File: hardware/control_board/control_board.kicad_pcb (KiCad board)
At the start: 2 copper layers, 80 x 80 mm, 126 parts, among them J1 SWD, J2 Panel, J3 Aux, J4 6.5/2mm, J5 USB_C, J6 RTD, J7 TC, J8 Conn_01x01, J9 Conn_01x01, Q1 2N7002A, Q2 IRF1018ESTRLPBF, SW1 Reset, SW2 Power, U1 STM32F103C8T6, U2 LMR38010SDDAR, U3 TLV76133DCYR, U4 USBLC6-2SC6, U5 MAX6675, U6 MCP6N11T-005E, U7 MCP6001T, U8 TLP183, Y1 8MHz

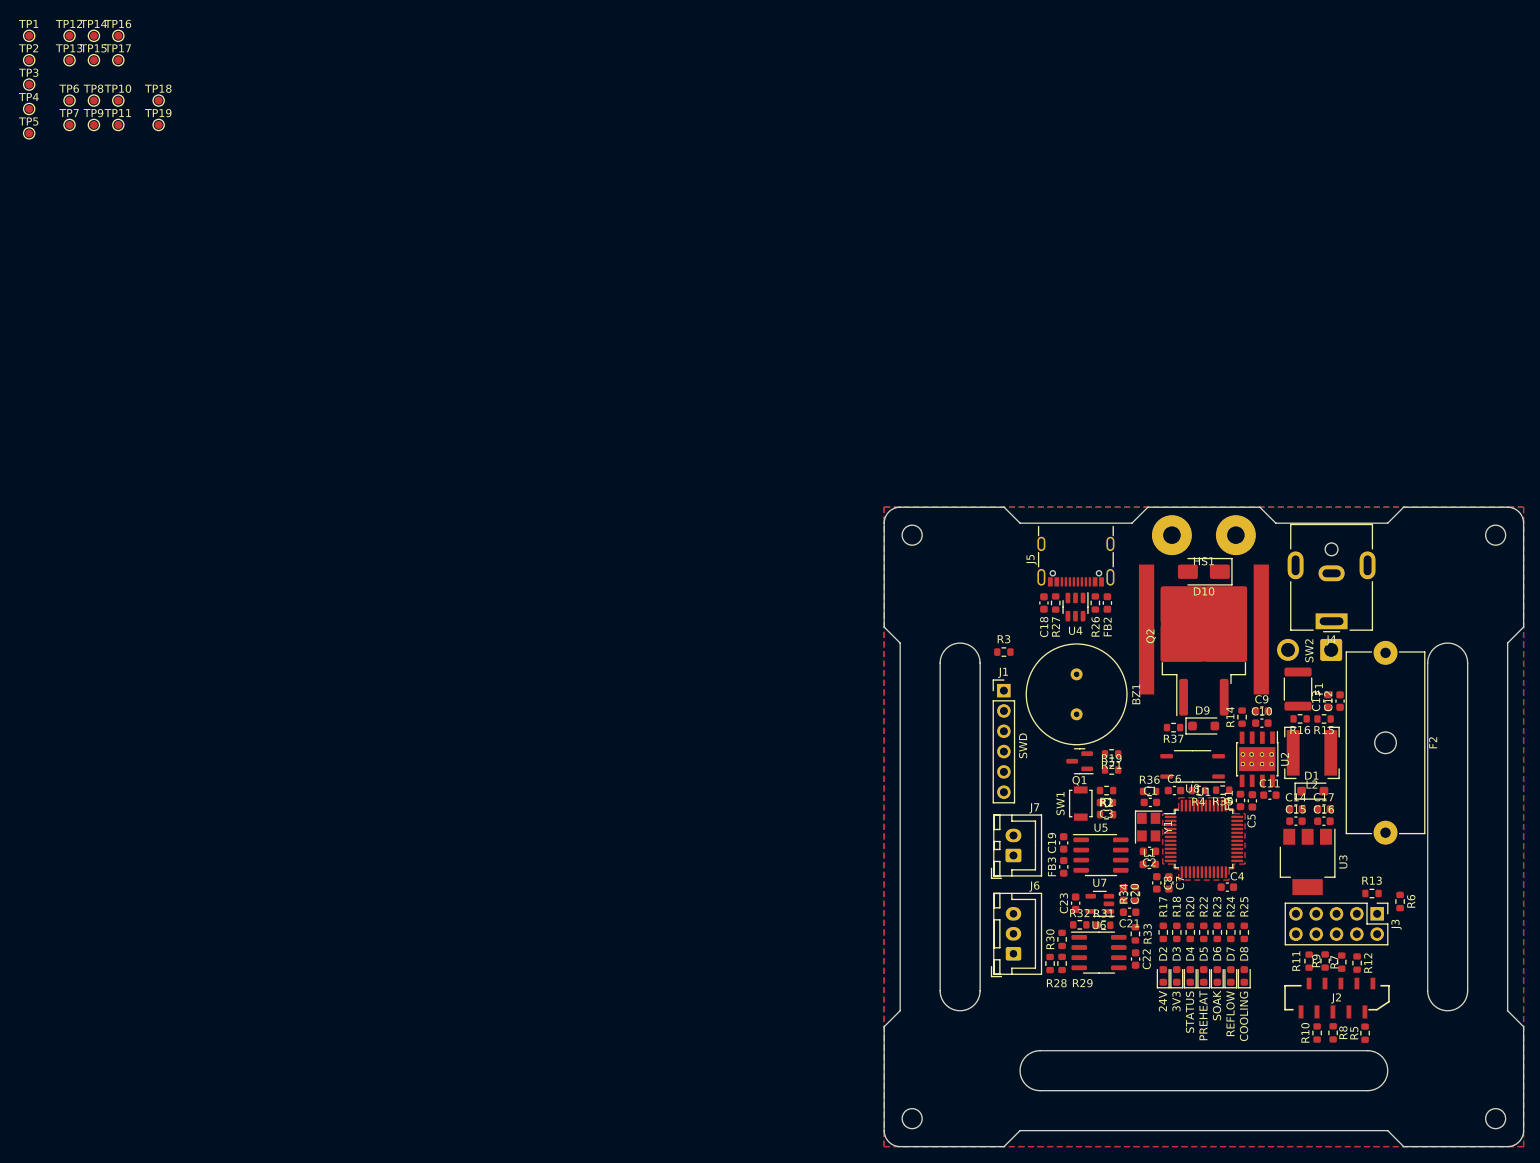
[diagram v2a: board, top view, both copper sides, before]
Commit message: Route control board PCB tracks
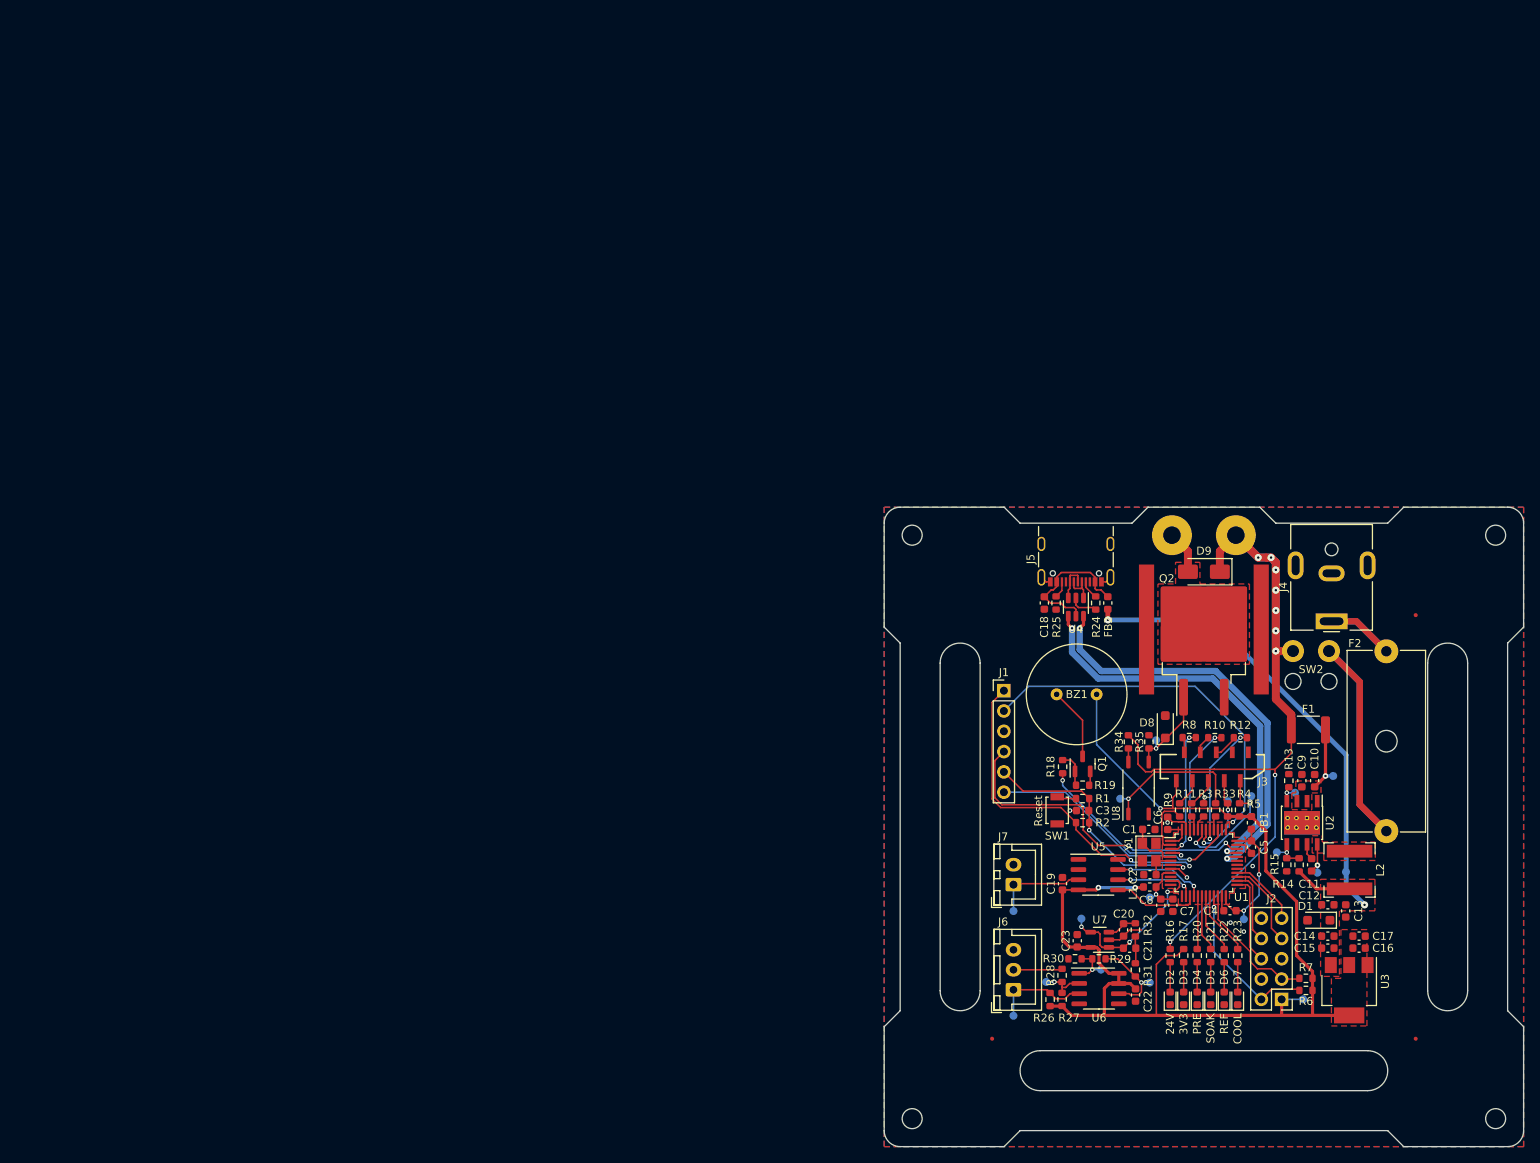
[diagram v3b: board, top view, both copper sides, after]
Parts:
- removed the D8 at (153.1, 118.6)
- removed FB3: 600R@100MHz, Inductor_SMD:L_0603_1608Metric
- removed the R25 at (153.1, 113.2)
- removed the R3 at (123.0, 78.1)
- removed TP19: TestPoint_Small, TestPoint:TestPoint_Pad_D1.0mm
- added FID1: Fiducial, Fiducial:Fiducial_0.5mm_Mask1mm, F.Cu at (121.5, 126.5)
- added FID2: Fiducial, Fiducial:Fiducial_0.5mm_Mask1mm, F.Cu at (174.5, 126.5)
- added FID3: Fiducial, Fiducial:Fiducial_0.5mm_Mask1mm, F.Cu at (174.5, 73.5)
- added NT1: NetTie_2, Local_Library:NetTie-2_SMD_Pad0.2mm, F.Cu at (156.9, 93.2)
- added NT2: NetTie_2, Local_Library:NetTie-2_SMD_Pad0.2mm, F.Cu at (156.6, 92.8)
- added REF**: MountingHole_2mm, MountingHole:MountingHole_2mm, F.Cu at (159.2, 81.8)
- added REF**: MountingHole_2mm, MountingHole:MountingHole_2mm, F.Cu at (163.7, 81.8)
- added REF**: WEEE-Logo_4.2x6mm_SilkScreen, Symbol:WEEE-Logo_4.2x6mm_SilkScreen, B.Cu at (132.2, 123.5)
- TP1, TP10, TP11, TP12, TP13, TP14, TP15, TP16, TP17, TP18, TP3, TP4, TP5, TP6, TP7, TP8, TP9: moved to B.Cu
- TP2: value TestPoint_Alt -> TestPoint_Small; moved to B.Cu
- moved TP1 187.9 mm to (153.0, 111.5), turned to 180 degrees
- moved TP10 186.1 mm to (160.4, 121.6), turned to 180 degrees
- moved TP9 182.4 mm to (165.8, 105.6), turned to 180 degrees
- moved TP7 182.0 mm to (162.2, 105.7), turned to 180 degrees
- moved TP5 181.9 mm to (164.2, 93.6), turned to 180 degrees
- moved TP14 177.4 mm to (141.2, 119.5), turned to 180 degrees
- moved TP6 176.1 mm to (159.4, 95.7), turned to 180 degrees
- moved TP4 175.4 mm to (153.9, 96.2), turned to 180 degrees
- moved TP8 175.4 mm to (157.1, 103.2), turned to 180 degrees
- moved TP2 175.0 mm to (141.2, 108.8), turned to 180 degrees
- moved TP3 174.7 mm to (151.0, 96.8), turned to 180 degrees
- moved TP12 170.1 mm to (128.3, 119.4), turned to 180 degrees
- moved TP15 169.8 mm to (135.1, 117.8), turned to 180 degrees
- moved TP16 163.5 mm to (132.7, 111.5), turned to 180 degrees
- moved TP13 159.0 mm to (124.2, 110.5), turned to 180 degrees
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- renumbered D9 to D8, D10 to D9, J3 to J2, J2 to J3, R7 to R12, R14 to R13, R15 to R14, R16 to R15, R17 to R16, R18 to R17, R19 to R18, R21 to R19, R22 to R21, R23 to R22, R24 to R23, R26 to R24, R27 to R25, R28 to R26, R29 to R27, R30 to R28, R31 to R29, R4 to R3, R32 to R30, R33 to R31, R34 to R32, R35 to R33, R36 to R34, R37 to R35, R5 to R4, R12 to R5, R13 to R7, R9 to R8, R8 to R9
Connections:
- C18 pad 1: +5V -> /USB Connector/VBUS
- C22 pad 1: VDDA -> +3.3V
- C23 pad 1: VDDA -> +3.3V
- D8 pad 1: Net-(D9-K) -> Net-(D8-K)
- FB2 pad 2: Net-(FB2-Pad2) -> /USB Connector/VBUS
- J1 pad 1: Net-(J1-Pin_1) -> VDD
- J2 pad 4: /GPIO_PA8 -> unconnected-(J2-Pin_4-Pad4)
- J2 pad 5: /SPI2_MOSI -> unconnected-(J2-Pin_5-Pad5)
- J2 pad 6: /GPIO_PA9 -> /SPI2_~{CS}
- J2 pad 8: /SPI2_~{CS} -> /SPI2_SCK
- J2 pad 9: /SPI2_SCK -> /SPI2_MOSI
- J3 pad 1: +3.3V -> GND
- J3 pad 10: GND -> +3.3V
- J3 pad 2: /LCD_SCL -> /LCD_SDA
- J3 pad 3: /LCD_SDA -> GND
- J3 pad 4: GND -> /LCD_SCL
- J3 pad 6: Net-(J2-Pin_6) -> Net-(J3-Pin_6)
- J3 pad 7: Net-(J2-Pin_7) -> Net-(J3-Pin_7)
- J3 pad 8: Net-(J2-Pin_8) -> Net-(J3-Pin_8)
- J3 pad 9: Net-(J2-Pin_9) -> Net-(J3-Pin_9)
- J5 pad A4: Net-(FB2-Pad2) -> /USB Connector/VBUS
- J5 pad A9: Net-(FB2-Pad2) -> /USB Connector/VBUS
- J5 pad B4: Net-(FB2-Pad2) -> /USB Connector/VBUS
- J5 pad B9: Net-(FB2-Pad2) -> /USB Connector/VBUS
- Q2 pad 1: Net-(D9-K) -> Net-(D8-K)
- R10 pad 2: Net-(J2-Pin_8) -> Net-(J3-Pin_7)
- R11 pad 2: Net-(J2-Pin_9) -> Net-(J3-Pin_6)
- R16 pad 1: +24V -> Net-(NT1-Pad1)
- R29 pad 2: Net-(R31-Pad2) -> Net-(R29-Pad2)
- R31 pad 1: Net-(R31-Pad2) -> Net-(R29-Pad2)
- R33 pad 2: Net-(R35-Pad2) -> Net-(R33-Pad2)
- R34 pad 1: +24V -> Net-(NT2-Pad1)
- R35 pad 1: Net-(D9-K) -> Net-(D8-K)
- R8 pad 2: Net-(J2-Pin_7) -> Net-(J3-Pin_9)
- R9 pad 2: Net-(J2-Pin_6) -> Net-(J3-Pin_8)
- TP10 pad 1: +5V -> +3.3V
- TP11 pad 1: +3.3V -> /Temperature Sensors/IN+
- TP12 pad 1: /Temperature Sensors/IN+ -> /Temperature Sensors/IN-
- TP13 pad 1: /Temperature Sensors/IN- -> Net-(J7-Pin_1)
- TP14 pad 1: Net-(J7-Pin_1) -> Net-(R29-Pad2)
- TP15 pad 1: Net-(R31-Pad2) -> Net-(U6-FG)
- TP16 pad 1: Net-(U6-FG) -> /PT
- TP17 pad 1: /PT -> Net-(R33-Pad2)
- TP18 pad 1: Net-(R35-Pad2) -> Net-(D8-K)
- TP2 pad 1: Net-(U1-PA15) -> VDDA
- TP3 pad 1: VDDA -> /LCD_SCL
- TP4 pad 1: /LCD_SCL -> /LCD_SDA
- TP5 pad 1: /LCD_SDA -> /Power Supply/VIN
- TP6 pad 1: /Power Supply/VIN -> /Power Supply/RT
- TP7 pad 1: /Power Supply/RT -> /Power Supply/SW
- TP8 pad 1: /Power Supply/SW -> /Power Supply/FB
- TP9 pad 1: /Power Supply/FB -> +5V
- U1 pad 13: /BUZZER -> unconnected-(U1-PA3-Pad13)
- U1 pad 2: /BUTTON_LEFT -> /BUTTON_UP
- U1 pad 29: /GPIO_PA8 -> unconnected-(U1-PA8-Pad29)
- U1 pad 3: /BUTTON_RIGHT -> /BUTTON_DOWN
- U1 pad 30: /GPIO_PA9 -> unconnected-(U1-PA9-Pad30)
- U1 pad 38: Net-(U1-PA15) -> unconnected-(U1-PA15-Pad38)
- U1 pad 4: unconnected-(U1-PC15-Pad4) -> /BUZZER
- U1 pad 45: /BUTTON_UP -> /BUTTON_RIGHT
- U1 pad 46: /BUTTON_DOWN -> /BUTTON_LEFT
- U4 pad 1: /USB Connector/DATA+ -> /USB Connector/DATA-
- U4 pad 3: /USB Connector/DATA- -> /USB Connector/DATA+
- U4 pad 4: /USB_D- -> /USB_D+
- U4 pad 5: +5V -> /USB Connector/VBUS
- U4 pad 6: /USB_D+ -> /USB_D-
- U5 pad 4: Net-(U5-VCC) -> +3.3V
- U6 pad 6: Net-(R31-Pad2) -> Net-(R29-Pad2)
- U6 pad 7: VDDA -> +3.3V
- U6 pad 8: VDDA -> +3.3V
- U7 pad 5: VDDA -> +3.3V
- U8 pad 1: Net-(R35-Pad2) -> Net-(R33-Pad2)
- U8 pad 4: Net-(D9-K) -> Net-(D8-K)
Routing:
- net +3.3V: track 0.00 -> 149.7 mm, vias 0 -> 3
- net +5V: track 0.00 -> 65.0 mm, vias 0 -> 2
- net VDD: track 0.00 -> 65.0 mm, vias 0 -> 4
- net +24V: track 0.00 -> 61.2 mm, vias 0 -> 7
- net /USB_D-: track 0.00 -> 52.6 mm, vias 0 -> 2
- net /USB_D+: track 0.00 -> 51.0 mm, vias 0 -> 2
- net Net-(SW2-A): track 0.00 -> 51.0 mm
- net /SWCLK: track 0.00 -> 47.0 mm, vias 0 -> 1
- net /SWDIO: track 0.00 -> 41.6 mm, vias 0 -> 2
- net /SWO: track 0.00 -> 32.3 mm, vias 0 -> 1
- net /NRST: track 0.00 -> 31.5 mm, vias 0 -> 2
- net Net-(NT1-Pad1): track 0.00 -> 27.2 mm, vias 0 -> 2
- net GND: track 0.00 -> 25.2 mm, vias 0 -> 7
- net /BUZZER: track 0.00 -> 21.4 mm, vias 0 -> 2
- net Net-(NT2-Pad1): track 0.00 -> 21.1 mm
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- added copper zone on F.Cu, net +3.3V
- added copper zone on F.Cu, net +5V
- added copper zone on F.Cu, net /Power Supply/SW
- added copper zone on F.Cu, net /Power Supply/VIN
- added copper zone on F.Cu, net Net-(D9-A)
- added copper zone on F.Cu, net VDD
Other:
- board text added: "20230911"
- board text added: "COOL"
- board text added: "PRE"
- board text added: "REF"
- board text added: "Reset"
- board text removed: "2023-08-06"
- board text removed: "Author: I. Kajdan"
- board text removed: "COOLING"
- board text removed: "PREHEAT"
- board text removed: "REFLOW"
- board text removed: "STATUS"
- board text removed: "SWD"

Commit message: Fix DRC errors
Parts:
- removed the G*** at (167.2, 113.0)
- removed the REF** at (159.2, 81.8)
- removed the REF** at (163.7, 81.8)
- removed the REF** at (132.2, 123.5)
- added REF**: OSHW-Logo2_7.3x6mm_SilkScreen, Local_Library:OSHW-Logo2_7.3x6mm_SilkScreen, B.Cu at (131.2, 123.6)
- J8, J9: footprint Local_Library:Pad_D5mm_H2.2mm -> Local_Library:Pad_D5mm_H2.2mm_Via
- SW2: footprint Connector_Wire:SolderWire-1sqmm_1x02_P5.4mm_D1.4mm_OD2.7mm -> Local_Library:SwitchWireRelief
- U8: footprint Package_SO:SOIC-4_4.55x3.7mm_P2.54mm -> Local_Library:SOIC-4_4.55x3.7mm_P2.54mm
- moved G*** 41.0 mm to (148.0, 117.5)
- moved SW2 4.50 mm to (159.2, 78.0), turned to 0 degrees
- moved TP12 1.45 mm to (129.3, 118.3)
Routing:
- net +24V: track 61.2 -> 59.9 mm, vias 7 -> 5
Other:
- board text added: "Author: I. Kajdan Promoter: A. Bondyra, Ph.D."
- board text added: "Control Board v${REVISION}"
- board text removed: "Promoter: A. Bondyra, Ph.D."
- board text removed: "v${REVISION}"

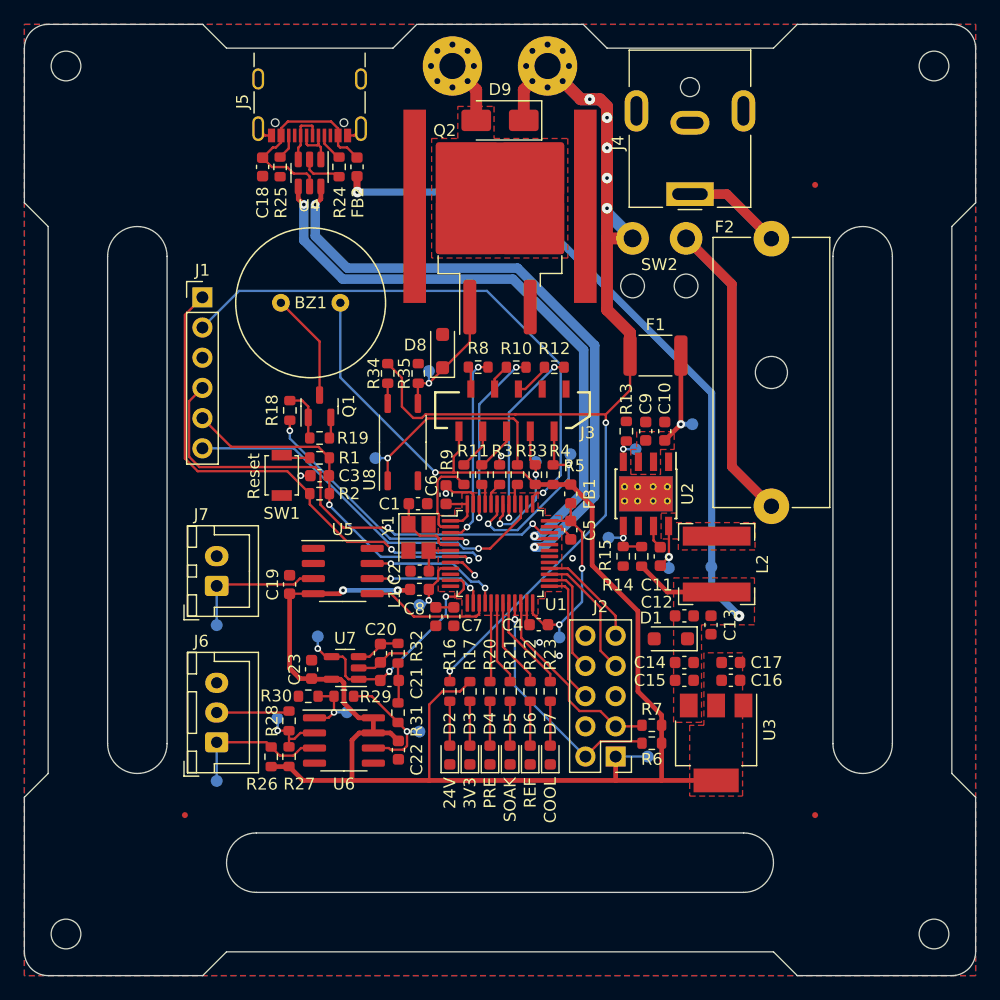
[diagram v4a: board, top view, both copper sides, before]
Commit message: Stitch the ground planes
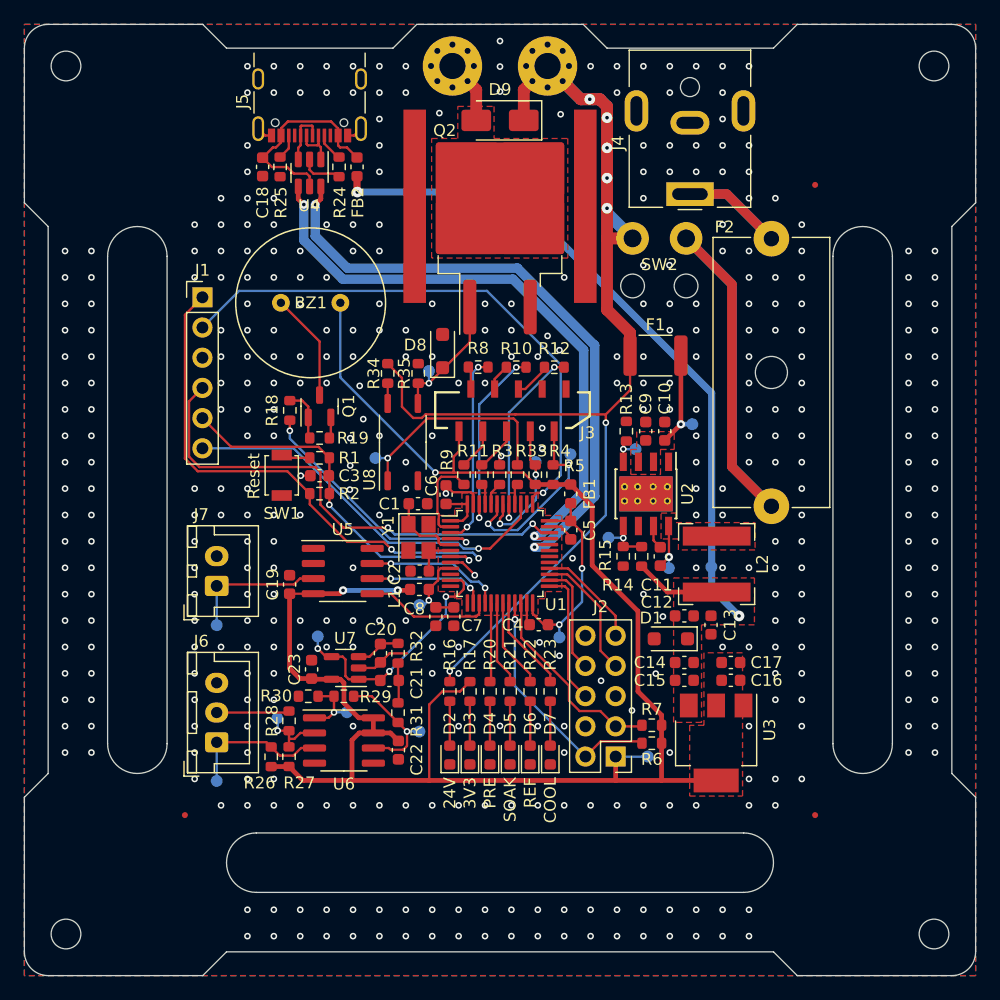
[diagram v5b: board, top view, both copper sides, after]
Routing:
- net GND: vias 7 -> 408

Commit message: Tidy up vias
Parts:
- moved TP9 5.61 mm to (169.6, 109.8)
- moved TP2 0.41 mm to (141.1, 108.4)
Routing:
- net +5V: track 65.0 -> 66.5 mm
- net GND: vias 408 -> 383
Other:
- board text added: "20230912"
- board text added: "Author: I. Kajdan"
- board text added: "Promoter: A. Bondyra, Ph.D."
- board text removed: "20230911"
- board text removed: "Author: I. Kajdan Promoter: A. Bondyra, Ph.D."

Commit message: Minor layout adjustments
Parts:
- C10: value 100n -> 100n/35V
- C9: value 4u7 -> 4u7/35V
- FB1, FB2: value 600R@100MHz -> 470R@100MHz
- J4: footprint Connector_BarrelJack:BarrelJack_CUI_PJ-063AH_Horizontal -> Local_Library:BarrelJack_CUI_PJ-063AH_Horizontal
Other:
- board text added: "20230913"
- board text removed: "20230912"
